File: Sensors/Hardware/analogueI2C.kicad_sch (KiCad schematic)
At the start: 100 parts, among them J10 1053131104, J11 1053131104, J12 1053131104, J13 1053131104, J14 1053131104, J3 1053131104, J4 1053131104, J5 1053131104, J6 1053131104, J7 1053131104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

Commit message: grouping layout
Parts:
- J10, J11, J12, J13, J14, J3, J4, J5, J6, J7, J8, J9: footprint CON_1053131104 -> iclr:1053131104
- U10, U9: footprint QFN_M06IRSNR_TEX -> iclr:ADS131M06IRSNR
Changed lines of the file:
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@@
       (effects (font (size 1.524 1.524)) (justify left))
     )
-    (property "Footprint" "CON_1053131104" (id 2) (at 264.16 112.014 0)
+    (property "Footprint" "iclr:1053131104" (id 2) (at 264.16 112.014 0)
       (effects (font (size 1.524 1.524)) hide)
     )
@@
       (effects (font (size 1.524 1.524)) (justify left))
     )
-    (property "Footprint" "CON_1053131104" (id 2) (at 168.91 75.184 0)
+    (property "Footprint" "iclr:1053131104" (id 2) (at 168.91 75.184 0)
       (effects (font (size 1.524 1.524)) hide)
     )
@@
       (effects (font (size 1.524 1.524)) (justify left))
     )
-    (property "Footprint" "CON_1053131104" (id 2) (at 215.9 75.184 0)
+    (property "Footprint" "iclr:1053131104" (id 2) (at 215.9 75.184 0)
       (effects (font (size 1.524 1.524)) hide)
     )
@@
       (effects (font (size 1.524 1.524)) (justify left))
     )
-    (property "Footprint" "CON_1053131104" (id 2) (at 262.89 150.114 0)
+    (property "Footprint" "iclr:1053131104" (id 2) (at 262.89 150.114 0)
       (effects (font (size 1.524 1.524)) hide)
     )
@@
       (effects (font (size 1.524 1.524)) (justify left))
     )
-    (property "Footprint" "CON_1053131104" (id 2) (at 171.45 152.654 0)
+    (property "Footprint" "iclr:1053131104" (id 2) (at 171.45 152.654 0)
       (effects (font (size 1.524 1.524)) hide)
     )
@@
       (effects (font (size 1.524 1.524)) (justify left))
     )
-    (property "Footprint" "CON_1053131104" (id 2) (at 265.43 72.644 0)
+    (property "Footprint" "iclr:1053131104" (id 2) (at 265.43 72.644 0)
       (effects (font (size 1.524 1.524)) hide)
     )
@@
       (effects (font (size 1.524 1.524)) (justify left))
     )
-    (property "Footprint" "CON_1053131104" (id 2) (at 170.18 113.284 0)
+    (property "Footprint" "iclr:1053131104" (id 2) (at 170.18 113.284 0)
       (effects (font (size 1.524 1.524)) hide)
     )
@@
       (effects (font (size 1.524 1.524)))
     )
-    (property "Footprint" "QFN_M06IRSNR_TEX" (id 2) (at 63.5 58.674 0)
+    (property "Footprint" "iclr:ADS131M06IRSNR" (id 2) (at 63.5 58.674 0)
       (effects (font (size 1.524 1.524)) hide)
     )
@@
       (effects (font (size 1.524 1.524)) (justify left))
     )
-    (property "Footprint" "CON_1053131104" (id 2) (at 217.17 113.284 0)
+    (property "Footprint" "iclr:1053131104" (id 2) (at 217.17 113.284 0)
       (effects (font (size 1.524 1.524)) hide)
     )
@@
       (effects (font (size 1.524 1.524)) (justify left))
     )
-    (property "Footprint" "CON_1053131104" (id 2) (at 167.64 35.814 0)
+    (property "Footprint" "iclr:1053131104" (id 2) (at 167.64 35.814 0)
       (effects (font (size 1.524 1.524)) hide)
     )
@@
       (effects (font (size 1.524 1.524)) (justify left))
     )
-    (property "Footprint" "CON_1053131104" (id 2) (at 264.16 34.544 0)
+    (property "Footprint" "iclr:1053131104" (id 2) (at 264.16 34.544 0)
       (effects (font (size 1.524 1.524)) hide)
     )
@@
       (effects (font (size 1.524 1.524)) (justify left))
     )
-    (property "Footprint" "CON_1053131104" (id 2) (at 212.09 37.084 0)
+    (property "Footprint" "iclr:1053131104" (id 2) (at 212.09 37.084 0)
       (effects (font (size 1.524 1.524)) hide)
     )
@@
       (effects (font (size 1.524 1.524)) (justify left))
     )
-    (property "Footprint" "CON_1053131104" (id 2) (at 215.9 151.384 0)
+    (property "Footprint" "iclr:1053131104" (id 2) (at 215.9 151.384 0)
       (effects (font (size 1.524 1.524)) hide)
     )
@@
       (effects (font (size 1.524 1.524)))
     )
-    (property "Footprint" "QFN_M06IRSNR_TEX" (id 2) (at 66.04 133.604 0)
+    (property "Footprint" "iclr:ADS131M06IRSNR" (id 2) (at 66.04 133.604 0)
       (effects (font (size 1.524 1.524)) hide)
     )

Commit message: nanofit placements
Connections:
- net +3V3: no longer C41.2, C42.2
- net GND: now also C41.2, C42.2
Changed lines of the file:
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@@
   (junction (at 196.85 157.48) (diameter 0) (color 0 0 0 0)
   )
+  (junction (at 119.38 160.02) (diameter 0) (color 0 0 0 0)
+  )
   (junction (at 157.48 44.45) (diameter 0) (color 0 0 0 0)
   )
@@
   )
   (junction (at 198.12 109.22) (diameter 0) (color 0 0 0 0)
+  )
+  (junction (at 116.84 85.09) (diameter 0) (color 0 0 0 0)
   )
   (junction (at 245.11 118.11) (diameter 0) (color 0 0 0 0)
@@
   (no_connect (at 30.48 97.79))
   (no_connect (at 33.02 172.72))
-  (wire (pts (xy 104.14 85.09) (xy 107.95 85.09))
+  (wire (pts (xy 104.14 85.09) (xy 116.84 85.09))
     (stroke (width 0) (type default) (color 0 0 0 0))
   )
@@
     (stroke (width 0) (type default) (color 0 0 0 0))
   )
-  (wire (pts (xy 116.84 87.63) (xy 116.84 82.55))
+  (wire (pts (xy 116.84 87.63) (xy 116.84 85.09))
     (stroke (width 0) (type default) (color 0 0 0 0))
   )
@@
     (stroke (width 0) (type default) (color 0 0 0 0))
   )
-  (wire (pts (xy 110.49 160.02) (xy 110.49 157.48))
-    (stroke (width 0) (type default) (color 0 0 0 0))
-  )
   (wire (pts (xy 205.74 152.4) (xy 205.74 160.02))
     (stroke (width 0) (type default) (color 0 0 0 0))
@@
     (stroke (width 0) (type default) (color 0 0 0 0))
   )
-  (wire (pts (xy 107.95 85.09) (xy 107.95 82.55))
-    (stroke (width 0) (type default) (color 0 0 0 0))
-  )
   (wire (pts (xy 187.96 43.18) (xy 193.04 43.18))
     (stroke (width 0) (type default) (color 0 0 0 0))
@@
     (stroke (width 0) (type default) (color 0 0 0 0))
   )
+  (wire (pts (xy 119.38 160.02) (xy 119.38 157.48))
+    (stroke (width 0) (type default) (color 0 0 0 0))
+  )
   (wire (pts (xy 199.39 35.56) (xy 201.93 35.56))
     (stroke (width 0) (type default) (color 0 0 0 0))
@@
     (stroke (width 0) (type default) (color 0 0 0 0))
   )
-  (wire (pts (xy 106.68 160.02) (xy 110.49 160.02))
-    (stroke (width 0) (type default) (color 0 0 0 0))
-  )
   (wire (pts (xy 151.13 109.22) (xy 152.4 109.22))
     (stroke (width 0) (type default) (color 0 0 0 0))
@@
     (stroke (width 0) (type default) (color 0 0 0 0))
   )
+  (wire (pts (xy 116.84 85.09) (xy 116.84 82.55))
+    (stroke (width 0) (type default) (color 0 0 0 0))
+  )
   (wire (pts (xy 198.12 119.38) (xy 198.12 116.84))
     (stroke (width 0) (type default) (color 0 0 0 0))
@@
     (stroke (width 0) (type default) (color 0 0 0 0))
   )
+  (wire (pts (xy 106.68 160.02) (xy 119.38 160.02))
+    (stroke (width 0) (type default) (color 0 0 0 0))
+  )
   (wire (pts (xy 149.86 71.12) (xy 151.13 71.12))
     (stroke (width 0) (type default) (color 0 0 0 0))
@@
     (stroke (width 0) (type default) (color 0 0 0 0))
   )
-  (wire (pts (xy 119.38 162.56) (xy 119.38 157.48))
-    (stroke (width 0) (type default) (color 0 0 0 0))
-  )
+  (wire (pts (xy 119.38 162.56) (xy 119.38 160.02))
+    (stroke (width 0) (type default) (color 0 0 0 0))
+  )

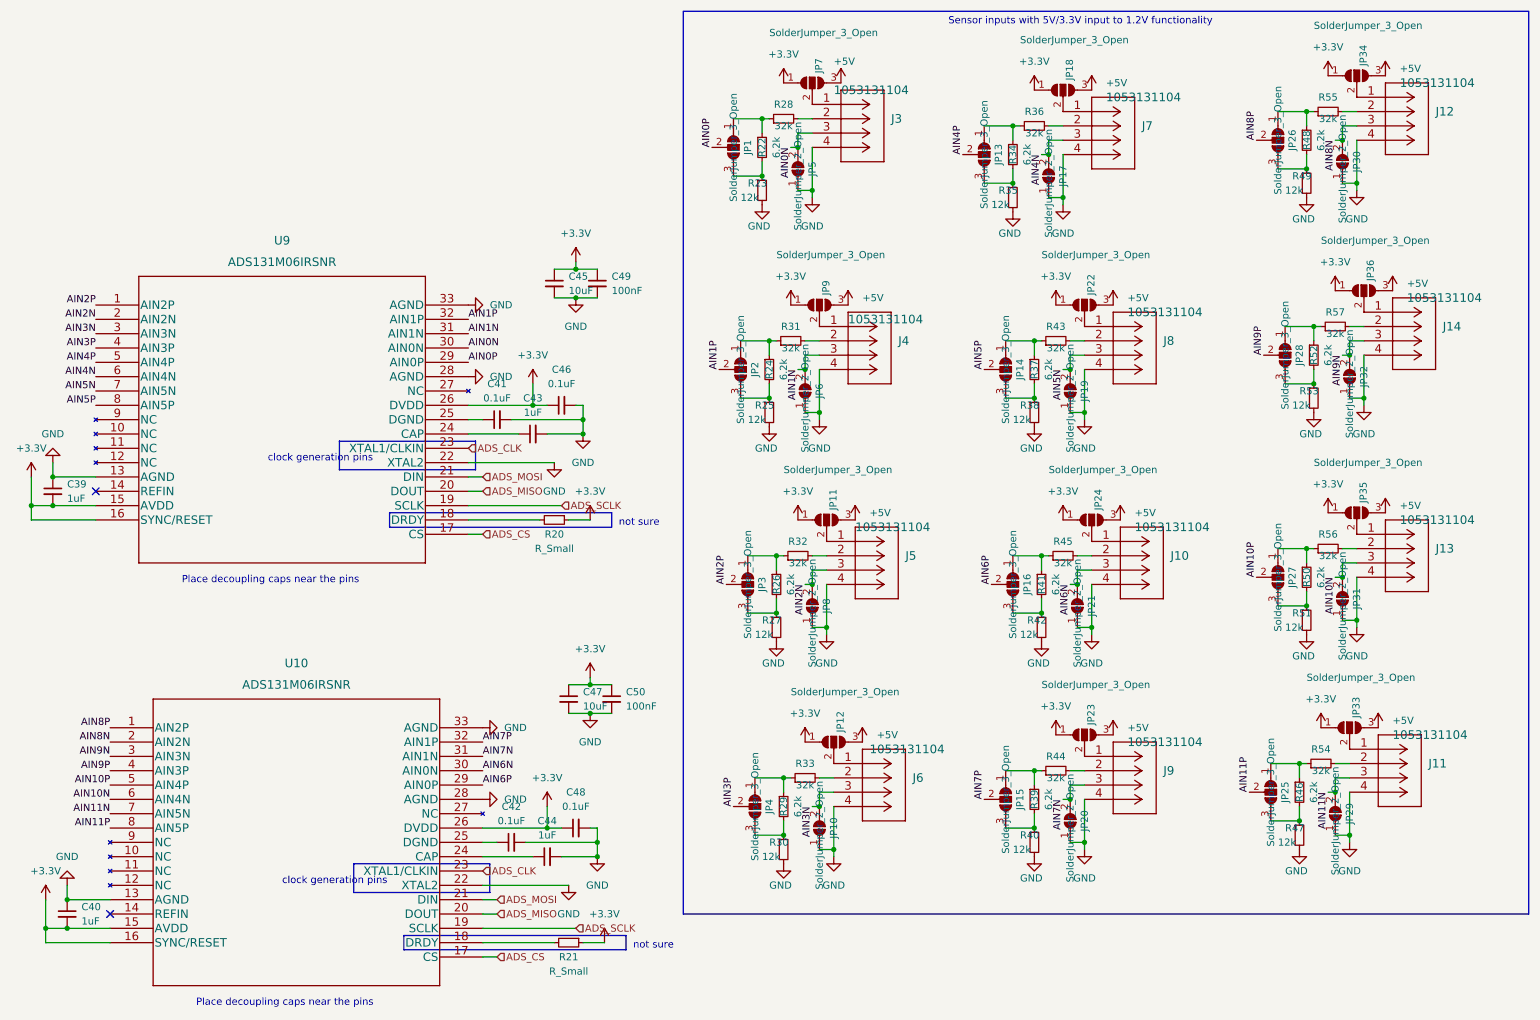
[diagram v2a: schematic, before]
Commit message: added low pass filters for ADC inputs
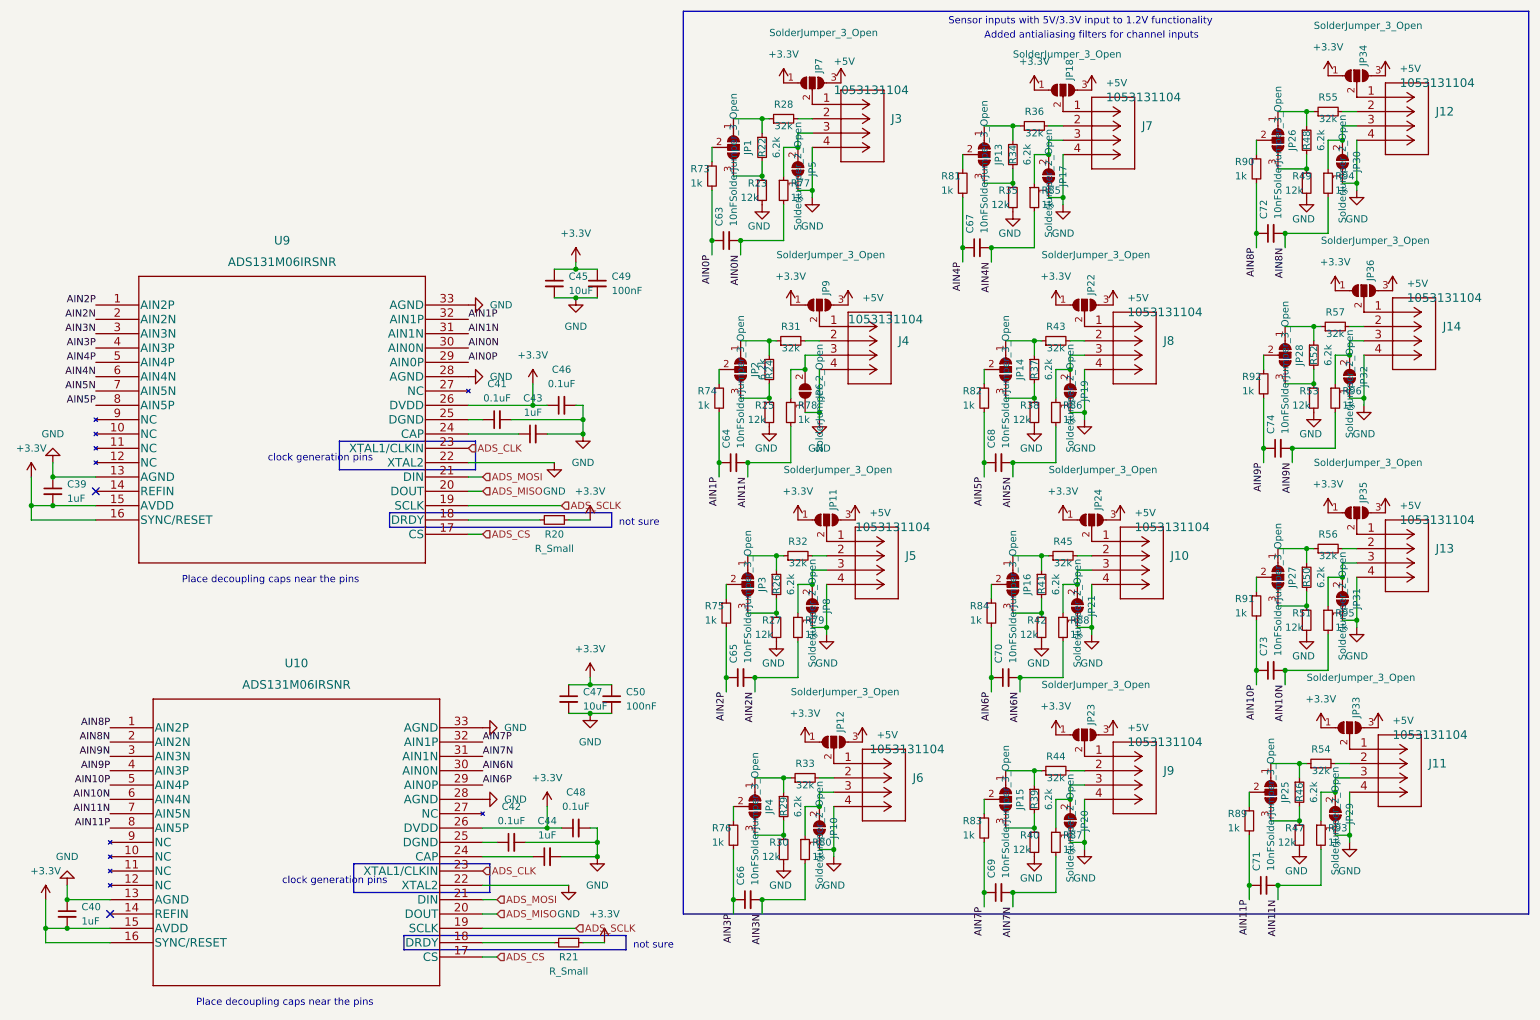
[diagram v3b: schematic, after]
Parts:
- added C63, C64, C65, C66, C67, C68, C69, C70, C71, C72, C73, C74: 10nF, Capacitor_SMD:C_0402_1005Metric, symbol Device:C_Small
- added R73, R74, R75, R76, R77, R78, R79, R80, R81, R82, R83, R84, R85, R86, R87, R88, R89, R90, R91, R92, R93, R94, R95, R96: 1k, Resistor_SMD:R_0402_1005Metric, symbol Device:R_Small
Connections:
- net AIN0N: now also C63.2, R77.2; no longer J3.3, JP5.2 (B)
- net AIN0P: now also C63.1, R73.2; no longer JP1.2 (C)
- net AIN10N: now also C73.2, R95.2; no longer J13.3, JP31.2 (B)
- net AIN10P: now also C73.1, R91.2; no longer JP27.2 (C)
- net AIN11N: now also C71.2, R93.2; no longer J11.3, JP29.2 (B)
- net AIN11P: now also C71.1, R89.2; no longer JP25.2 (C)
- net AIN1N: now also C64.2, R78.2; no longer J4.3, JP6.2 (B)
- net AIN1P: now also C64.1, R74.2; no longer JP2.2 (C)
- net AIN2N: now also C65.2, R79.2; no longer J5.3, JP8.2 (B)
- net AIN2P: now also C65.1, R75.2; no longer JP3.2 (C)
- net AIN3N: now also C66.2, R80.2; no longer J6.3, JP10.2 (B)
- net AIN3P: now also C66.1, R76.2; no longer JP4.2 (C)
- net AIN4N: now also C67.2, R85.2; no longer J7.3, JP17.2 (B)
- net AIN4P: now also C67.1, R81.2; no longer JP13.2 (C)
- net AIN5N: now also C68.2, R86.2; no longer J8.3, JP19.2 (B)
- net AIN5P: now also C68.1, R82.2; no longer JP14.2 (C)
- net AIN6N: now also C70.2, R88.2; no longer J10.3, JP21.2 (B)
- net AIN6P: now also C70.1, R84.2; no longer JP16.2 (C)
- net AIN7N: now also C69.2, R87.2; no longer J9.3, JP20.2 (B)
- net AIN7P: now also C69.1, R83.2; no longer JP15.2 (C)
- net AIN8N: now also C72.2, R94.2; no longer J12.3, JP30.2 (B)
- net AIN8P: now also C72.1, R90.2; no longer JP26.2 (C)
- net AIN9N: now also C74.2, R96.2; no longer J14.3, JP32.2 (B)
- net AIN9P: now also C74.1, R92.2; no longer JP28.2 (C)
- new net: JP2.2 (C), R74.1
- new net: JP4.2 (C), R76.1
- new net: JP27.2 (C), R91.1
- new net: J9.3, JP20.2 (B), R87.1
- new net: JP25.2 (C), R89.1
- new net: J6.3, JP10.2 (B), R80.1
- new net: J13.3, JP31.2 (B), R95.1
- new net: J10.3, JP21.2 (B), R88.1
- new net: J12.3, JP30.2 (B), R94.1
- new net: J7.3, JP17.2 (B), R85.1
- new net: J3.3, JP5.2 (B), R77.1
- new net: JP1.2 (C), R73.1
- new net: J4.3, JP6.2 (B), R78.1
- new net: J8.3, JP19.2 (B), R86.1
- new net: J11.3, JP29.2 (B), R93.1
- new net: J5.3, JP8.2 (B), R79.1
- new net: JP3.2 (C), R75.1
- new net: JP14.2 (C), R82.1
- new net: J14.3, JP32.2 (B), R96.1
- new net: JP13.2 (C), R81.1
- new net: JP28.2 (C), R92.1
- new net: JP15.2 (C), R83.1
- new net: JP26.2 (C), R90.1
- new net: JP16.2 (C), R84.1
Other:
- note added: "Added antialiasing filters for channel inputs"

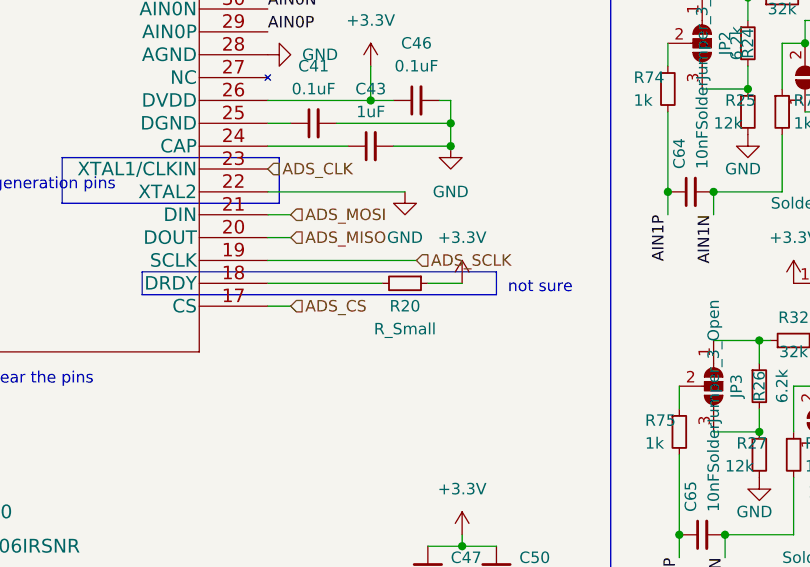
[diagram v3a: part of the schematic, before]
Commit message: 10v rail layout, adc update
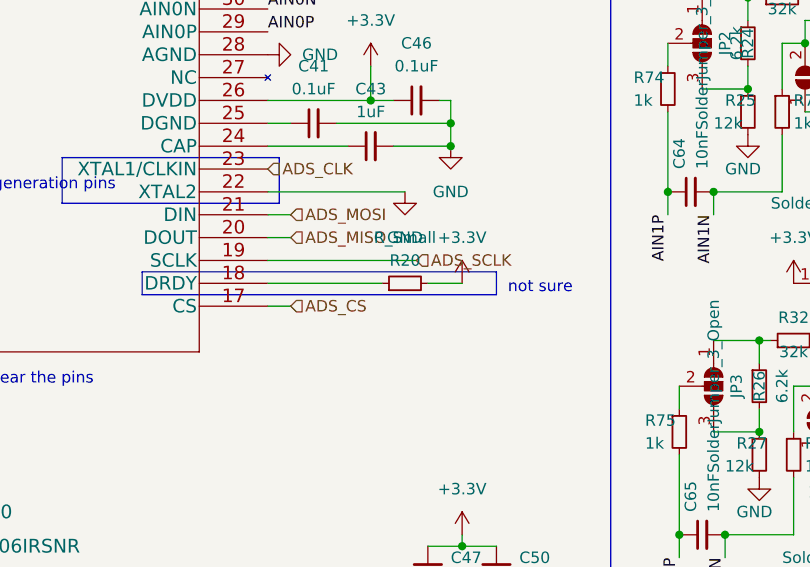
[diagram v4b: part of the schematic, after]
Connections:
- net +3V3: now also R20.2; no longer R20.1
- net at U9.18 (DRDY): now also R20.1; no longer R20.2
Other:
- moved on the sheet: R20
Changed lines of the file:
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@@
     (pin "2")
   )
-  (symbol (lib_id "Device:R_Small") (at 111.76 102.87 270) (unit 1)
+  (symbol (lib_id "Device:R_Small") (at 111.76 102.87 90) (unit 1)
     (in_bom yes) (on_board yes)
-    (property "Reference" "R20" (id 0) (at 111.76 105.41 90))
-    (property "Value" "R_Small" (id 1) (at 111.76 107.95 90))
+    (property "Reference" "R20" (id 0) (at 111.76 100.33 90))
+    (property "Value" "R_Small" (id 1) (at 111.76 97.79 90))
     (property "Footprint" "Resistor_SMD:R_0603_1608Metric" (id 2) (at 111.76 102.87 0)
       (effects (font (size 1.27 1.27)) hide)
